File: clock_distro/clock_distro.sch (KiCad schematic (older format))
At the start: 37 parts, among them J1 SMA, J10 SMA, J2 SMA, J3 SMA, J4 SMA, J5 SMA, J6 SMA, J7 SMA, J8 SMA, J9 SMA, P1 CONN_01X02, U1 CDCLVC1108

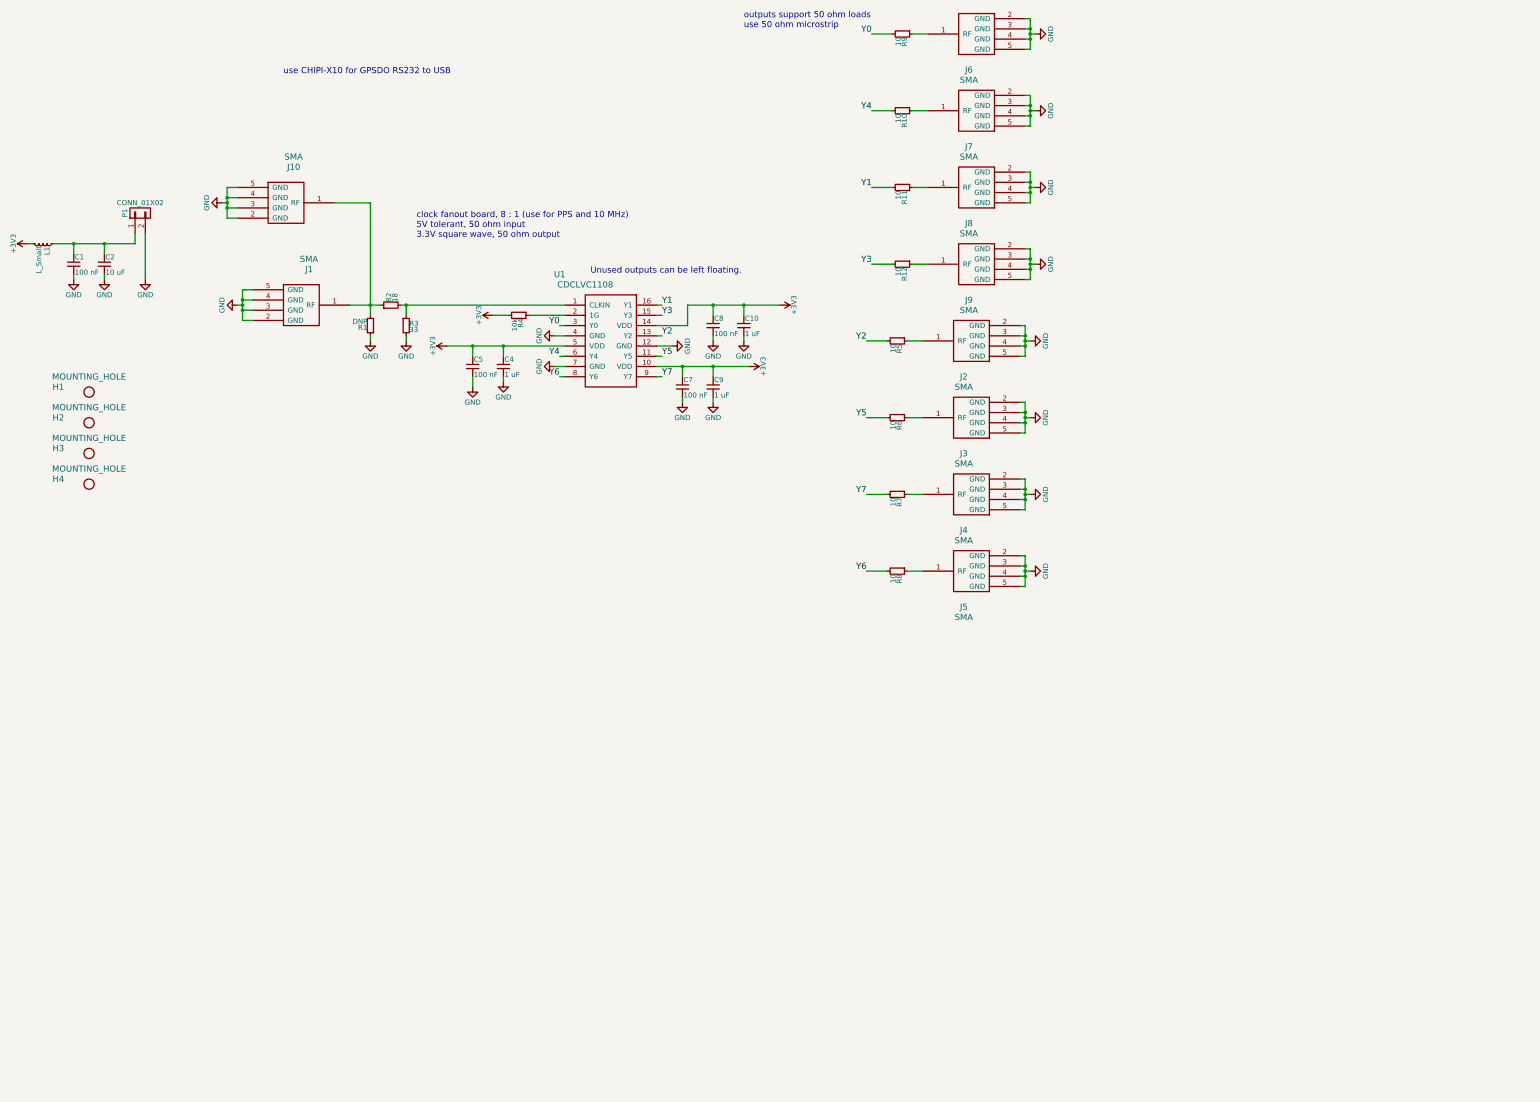
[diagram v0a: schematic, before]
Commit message: added bc637 pcie dsub15 clock/pps breakout
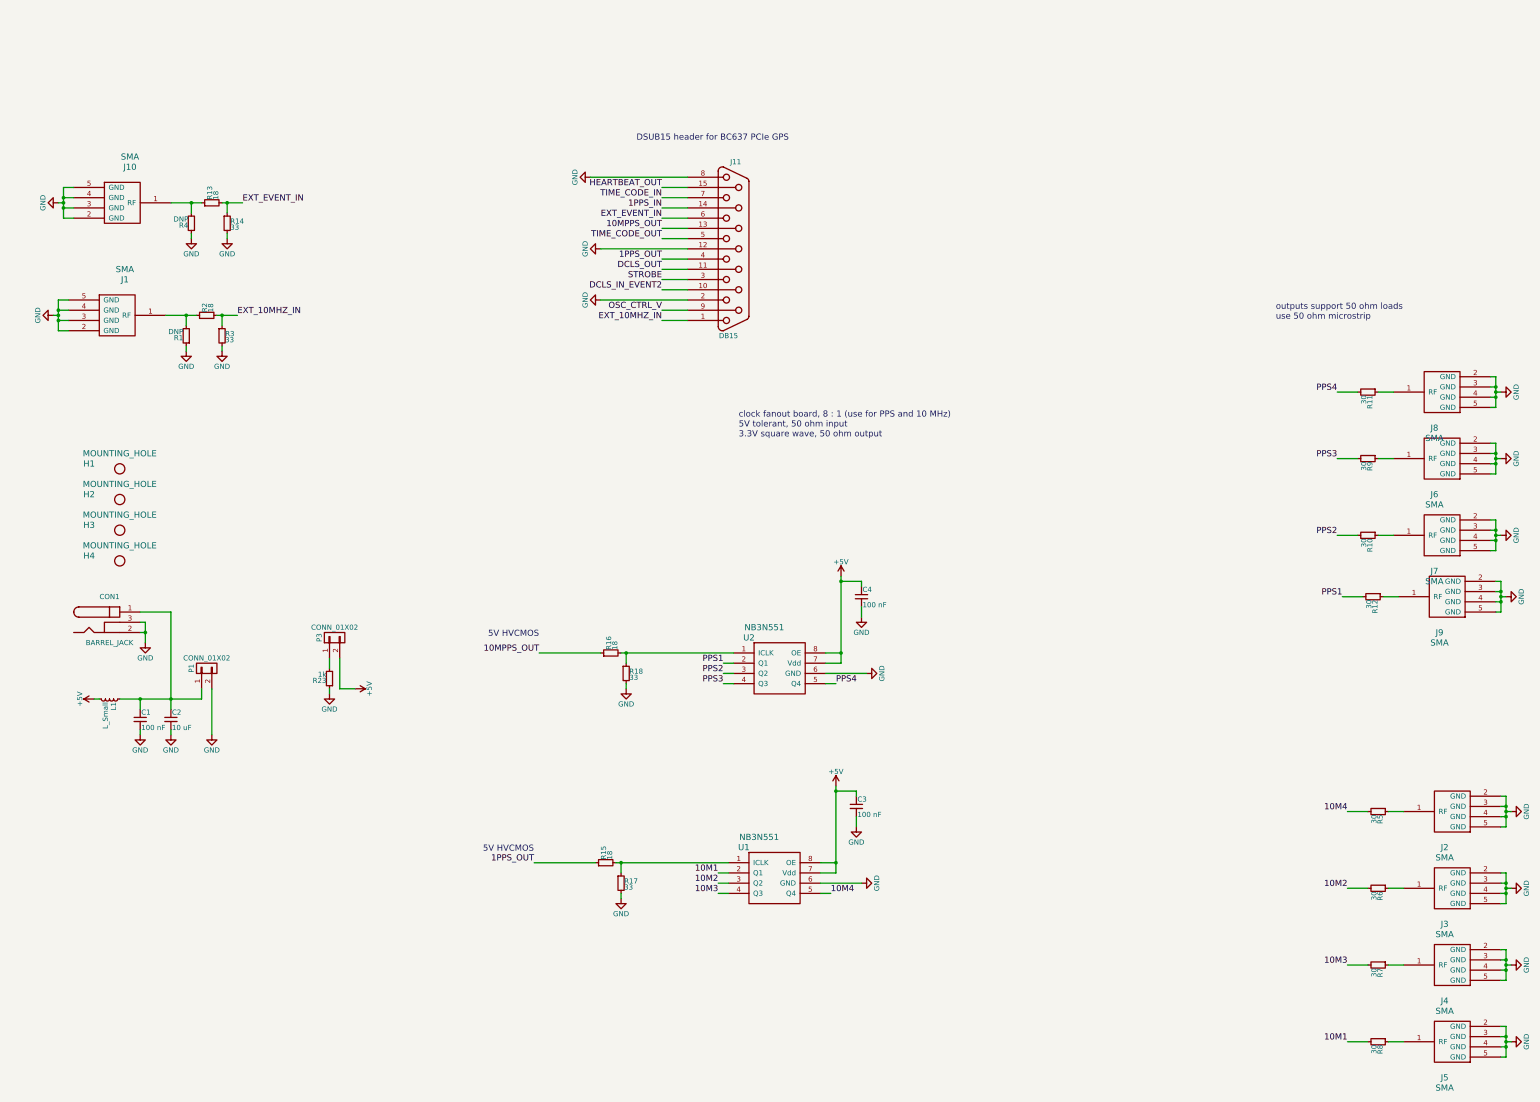
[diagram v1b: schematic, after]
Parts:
- removed C10, C9: 1 uF, Capacitors_SMD:C_0603, symbol C_Small
- removed C5, C7, C8: 100 nF, Capacitors_SMD:C_0603, symbol C_Small
- removed U1: CDCLVC1108, Housings_SSOP:TSSOP-16_4.4x5mm_Pitch0.65mm, symbol CDCLVC1108
- added C3: 100 nF, Capacitors_SMD:C_0603, symbol C_Small
- added CON1: BARREL_JACK, Connect:BARREL_JACK, symbol BARREL_JACK
- added J11: DB15, Connect:DB15FC, symbol DB15
- added P3: CONN_01X02, Connect:PINHEAD1-2, symbol CONN_01X02
- added R13, R15, R16: 18, Resistors_SMD:R_0603, symbol R_Small
- added R14, R17, R18: 33, Resistors_SMD:R_0603, symbol R_Small
- added R23: 1k, Resistors_SMD:R_0603, symbol R_Small
- added U1, U2: NB3N551, Housings_SOIC:SOIC-8_3.9x4.9mm_Pitch1.27mm, symbol NB3N551
- C4: value 1 uF -> 100 nF
- R10, R11, R12, R5, R6, R7, R8, R9: value 10 -> 30
- R4: value 10k -> DNP
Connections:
- net GND: now also R4.1, C3.2, CON1.2, CON1.3, J11.12 (P12), J11.2, J11.8, R14.2, R17.2, R18.2, R23.1, U1.6 (GND), U2.6 (GND)
- net EXT_10MHZ_IN: now reaches R2.2, R3.1
- net EXT_10MHZ_IN: now also J11.1
- net at C1.1, C2.1, L1.1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: now also CON1.1
- net at J1.1 (RF), R1.2, R2.1: no longer J10.1 (RF)
- net +3V3 renamed +5V
- net +5V: now also C3.1, P3.2 (P2), U1.7 (Vdd), U1.8 (OE), U2.7 (Vdd), U2.8 (OE); no longer R4.2
- net Y0 renamed PPS3
- net PPS3: now also U2.4 (Q3)
- net Y1 renamed PPS4
- net PPS4: now also U2.5 (Q4)
- net Y2 renamed 10M4
- net 10M4: now also U1.5 (Q4)
- net Y3 renamed PPS1
- net PPS1: now also U2.2 (Q1)
- net Y4 renamed PPS2
- net PPS2: now also U2.3 (Q2)
- net Y5 renamed 10M2
- net 10M2: now also U1.3 (Q2)
- net Y6 renamed 10M1
- net 10M1: now also U1.2 (Q1)
- net Y7 renamed 10M3
- net 10M3: now also U1.4 (Q3)
- new net: R16.2, R18.1, U2.1 (ICLK)
- new net: R15.2, R17.1, U1.1 (ICLK)
- new net: J10.1 (RF), R13.1, R4.2
- new net: P3.1 (P1), R23.2
- new net 10MPPS_OUT: J11.13 (P13), R16.1
- new net 1PPS_IN: J11.14 (P14)
- new net 1PPS_OUT: J11.4, R15.1
- new net DCLS_IN_EVENT2: J11.10 (P10)
- new net DCLS_OUT: J11.11 (P111)
- new net EXT_EVENT_IN: J11.6, R13.2, R14.1
- new net HEARTBEAT_OUT: J11.15 (P15)
- new net OSC_CTRL_V: J11.9 (P9)
- new net STROBE: J11.3
- new net TIME_CODE_IN: J11.7
- new net TIME_CODE_OUT: J11.5
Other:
- note added: "5V HVCMOS"
- note added: "DSUB15 header for BC637 PCIe GPS"
- note removed: "Unused outputs can be left floating."
- note removed: "use CHIPI-X10 for GPSDO RS232 to USB"
- moved on the sheet: C1, C2, H1, H2, H3, H4, J1, J2, J3, J4, J5, J6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

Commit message: length tuned clock/pps traces, switch dsub15 connector to male
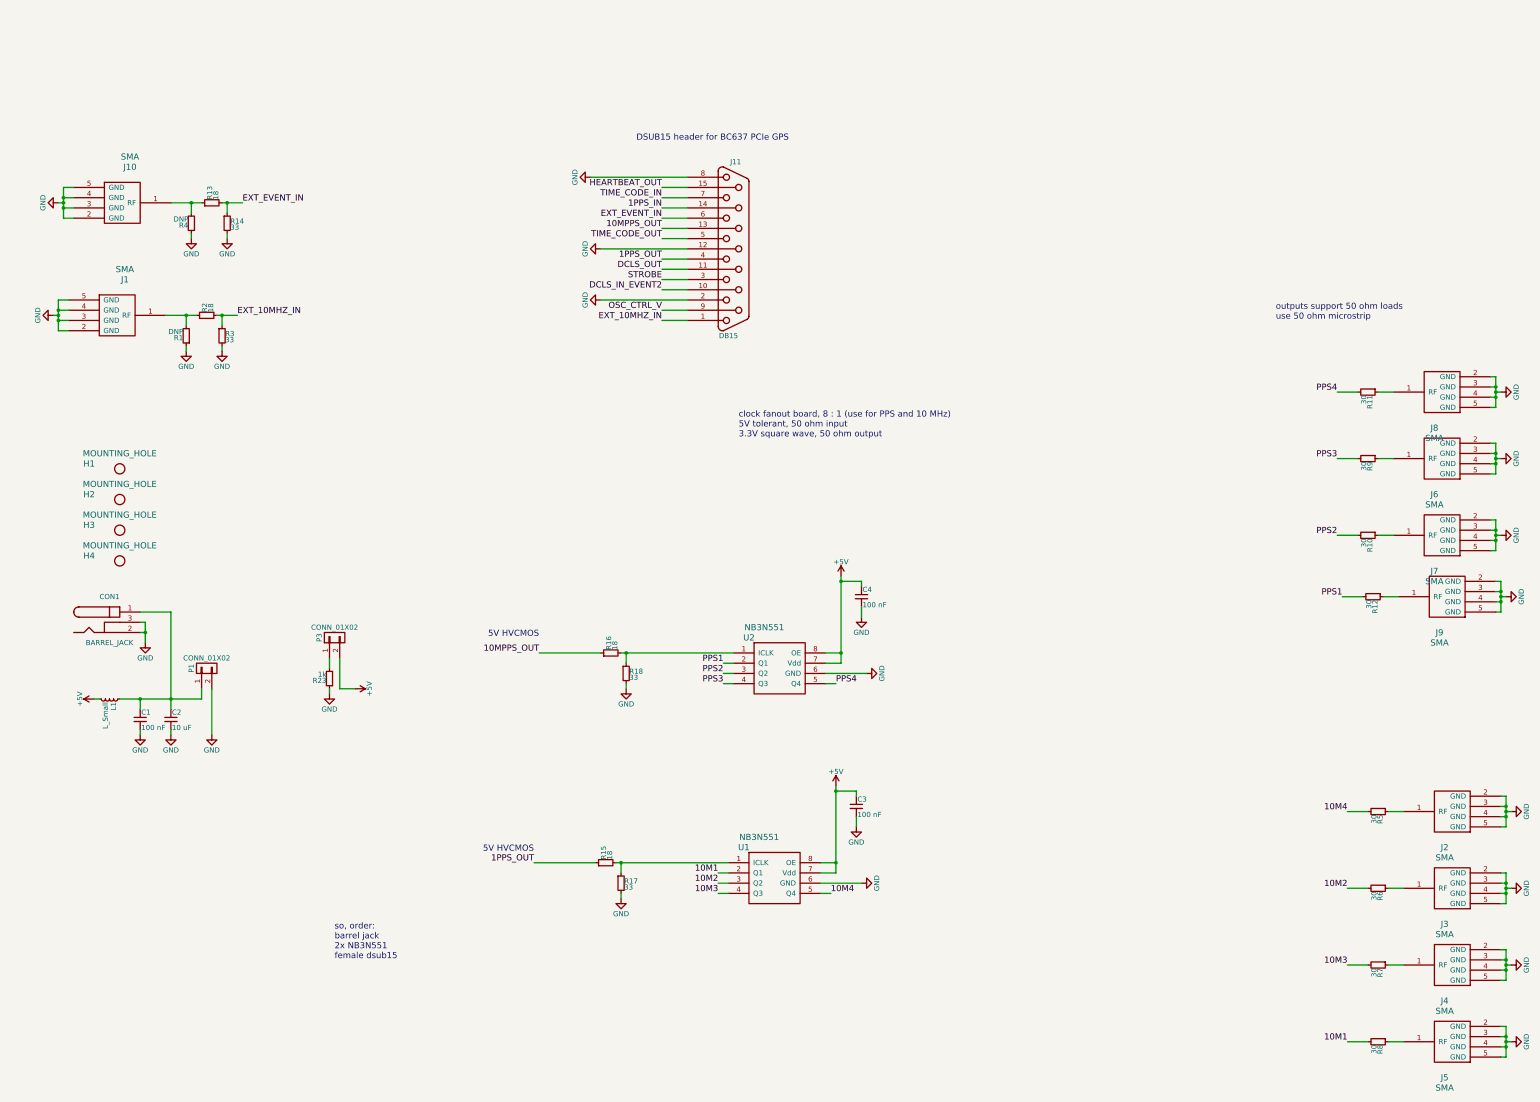
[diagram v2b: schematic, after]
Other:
- note added: "so, order:\nbarrel jack\n2x NB3N551\nfemale dsub15"
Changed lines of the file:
@@
 Connection ~ 2250 7250
 Wire Wire Line
-	2250 6400 2250 7250
-Wire Wire Line
-	2250 7250 2250 7350
+	2250 6400 2250 7350
 Wire Wire Line
 	2250 7600 2250 7550
@@
 	2550 7250 2550 7150
 Wire Wire Line
-	1750 7250 1950 7250
-Wire Wire Line
-	1950 7250 2250 7250
-Wire Wire Line
-	2250 7250 2550 7250
+	1750 7250 2550 7250
 Wire Wire Line
 	2650 7150 2650 7600
@@
 $EndComp
 Wire Wire Line
-	1100 3500 1150 3500
-Wire Wire Line
-	1150 3350 1150 3450
-Wire Wire Line
-	1150 3450 1150 3500
-Wire Wire Line
-	1150 3500 1150 3550
-Wire Wire Line
-	1150 3550 1150 3650
+	1150 3500 1100 3500
+Wire Wire Line
+	1150 3350 1150 3650
 Wire Wire Line
 	1150 3350 1250 3350
@@
 	2400 3800 2400 3850
 Wire Wire Line
-	2200 3500 2400 3500
-Wire Wire Line
-	2400 3500 2500 3500
+	2200 3500 2500 3500
 $Comp
 L GND #PWR06
@@
 	15150 4850 15200 4850
 Wire Wire Line
-	15200 4750 15200 4850
-Wire Wire Line
-	15200 4850 15200 4900
-Wire Wire Line
-	15200 4900 15200 4950
-Wire Wire Line
-	15200 4950 15200 5050
+	15200 4750 15200 5050
 Wire Wire Line
 	15200 4900 15250 4900
@@
 	15150 5600 15200 5600
 Wire Wire Line
-	15200 5500 15200 5600
-Wire Wire Line
-	15200 5600 15200 5650
-Wire Wire Line
-	15200 5650 15200 5700
-Wire Wire Line
-	15200 5700 15200 5800
+	15200 5500 15200 5800
 Wire Wire Line
 	15200 5650 15250 5650
@@
 	15150 4200 15200 4200
 Wire Wire Line
-	15200 4100 15200 4200
-Wire Wire Line
-	15200 4200 15200 4250
-Wire Wire Line
-	15200 4250 15200 4300
-Wire Wire Line
-	15200 4300 15200 4400
+	15200 4100 15200 4400
 Wire Wire Line
 	15200 4250 15250 4250
@@
 	15200 6200 15250 6200
 Wire Wire Line
-	15250 6100 15250 6200
-Wire Wire Line
-	15250 6200 15250 6250
-Wire Wire Line
-	15250 6250 15250 6300
-Wire Wire Line
-	15250 6300 15250 6400
+	15250 6100 15250 6400
 Wire Wire Line
 	15250 6250 15300 6250
@@
 	15250 8300 15300 8300
 Wire Wire Line
-	15300 8200 15300 8300
-Wire Wire Line
-	15300 8300 15300 8350
-Wire Wire Line
-	15300 8350 15300 8400
-Wire Wire Line
-	15300 8400 15300 8500
+	15300 8200 15300 8500
 Wire Wire Line
 	15300 8350 15350 8350
@@
 	15250 9050 15300 9050
 Wire Wire Line
-	15300 8950 15300 9050
-Wire Wire Line
-	15300 9050 15300 9100
-Wire Wire Line
-	15300 9100 15300 9150
-Wire Wire Line
-	15300 9150 15300 9250
+	15300 8950 15300 9250
 Wire Wire Line
 	15300 9100 15350 9100
@@
 	15250 9800 15300 9800
 Wire Wire Line
-	15300 9700 15300 9800
-Wire Wire Line
-	15300 9800 15300 9850
-Wire Wire Line
-	15300 9850 15300 9900
-Wire Wire Line
-	15300 9900 15300 10000
+	15300 9700 15300 10000
 Wire Wire Line
 	15300 9850 15350 9850
@@
 	15250 10550 15300 10550
 Wire Wire Line
-	15300 10450 15300 10550
-Wire Wire Line
-	15300 10550 15300 10600
-Wire Wire Line
-	15300 10600 15300 10650
-Wire Wire Line
-	15300 10650 15300 10750
+	15300 10450 15300 10750
 Wire Wire Line
 	15300 10600 15350 10600
@@
 EXT_10MHZ_IN
 Wire Wire Line
-	2700 3500 2750 3500
-Wire Wire Line
-	2750 3500 2900 3500
+	2700 3500 2900 3500
 Text Label 5850 6800 2    60   ~ 0
 10MPPS_OUT
@@
 Connection ~ 6700 6800
 Wire Wire Line
-	6650 6800 6700 6800
-Wire Wire Line
-	6700 6800 7750 6800
+	6650 6800 7750 6800
 Wire Wire Line
 	5850 6800 6450 6800
@@
 	9050 7000 8650 7000
 Wire Wire Line
-	8650 6900 8800 6900
-Wire Wire Line
-	8800 6900 8800 6800
-Wire Wire Line
-	8800 6800 8800 6100
-Wire Wire Line
-	8800 6100 8800 6050
+	8800 6900 8650 6900
+Wire Wire Line
+	8800 6050 8800 6900
 $Comp
 L C_Small C4
@@
 Connection ~ 6650 8850
 Wire Wire Line
-	6600 8850 6650 8850
-Wire Wire Line
-	6650 8850 7700 8850
+	6600 8850 7700 8850
 Wire Wire Line
 	5800 8850 6400 8850
@@
 	9000 9050 8600 9050
 Wire Wire Line
-	8600 8950 8750 8950
-Wire Wire Line
-	8750 8950 8750 8850
-Wire Wire Line
-	8750 8850 8750 8150
-Wire Wire Line
-	8750 8150 8750 8100
+	8750 8950 8600 8950
+Wire Wire Line
+	8750 8100 8750 8950
 $Comp
 L C_Small C3
@@
 $EndComp
 Wire Wire Line
-	1150 2400 1200 2400
-Wire Wire Line
-	1200 2250 1200 2350
-Wire Wire Line
-	1200 2350 1200 2400
-Wire Wire Line
-	1200 2400 1200 2450
-Wire Wire Line
-	1200 2450 1200 2550
+	1200 2400 1150 2400
+Wire Wire Line
+	1200 2250 1200 2550
 Wire Wire Line
 	1200 2250 1300 2250
@@
 	2450 2700 2450 2750
 Wire Wire Line
-	2250 2400 2450 2400
-Wire Wire Line
-	2450 2400 2550 2400
+	2250 2400 2550 2400
 $Comp
 L R_Small R13
@@
 	2450 2400 2450 2500
 Wire Wire Line
-	2750 2400 2800 2400
-Wire Wire Line
-	2800 2400 2950 2400
+	2750 2400 2950 2400
 $Comp
 L BARREL_JACK CON1
@@
 	1950 6600 2000 6600
 Wire Wire Line
-	2000 6500 2000 6600
-Wire Wire Line
-	2000 6600 2000 6700
+	2000 6500 2000 6700
 Wire Wire Line
 	1950 6500 2000 6500
@@
 Wire Wire Line
 	3900 7150 3900 6850
+Text Notes 3850 9800 0    60   ~ 0
+so, order:\nbarrel jack\n2x NB3N551\nfemale dsub15
 $EndSCHEMATC

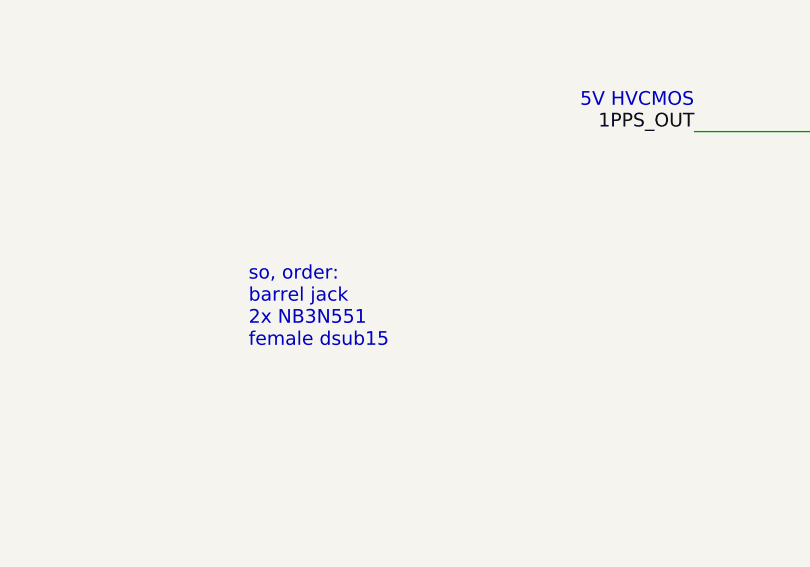
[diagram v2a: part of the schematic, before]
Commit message: fixed dsub 15 connector footprint - moved mounting holes
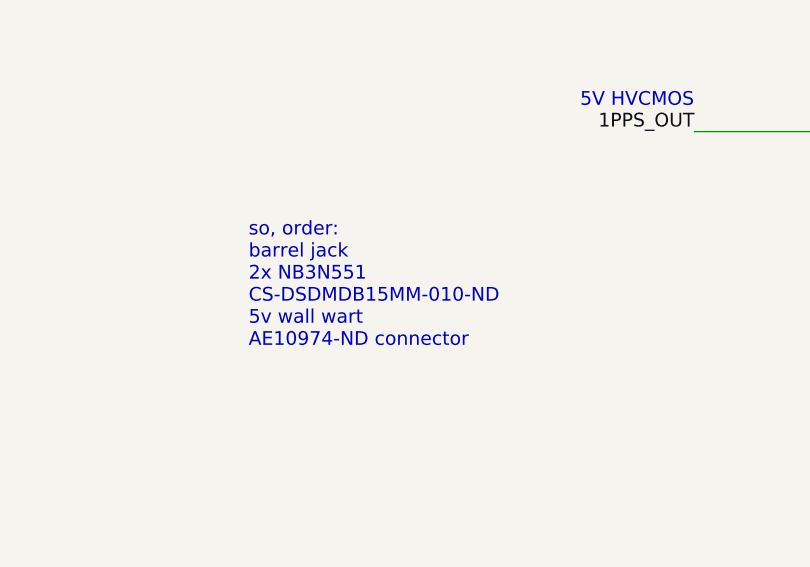
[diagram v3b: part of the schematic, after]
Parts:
- J11: footprint Connect:DB15FC -> Connect:DB15MC
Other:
- note added: "so, order:\nbarrel jack\n2x NB3N551\nCS-DSDMDB15MM-010-ND\n5v wall wart\nAE10974-ND connector"
- note removed: "so, order:\nbarrel jack\n2x NB3N551\nfemale dsub15"
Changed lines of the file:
@@
 F 0 "J11" H 7770 3700 50  0000 C CNN
 F 1 "DB15" H 7700 2000 50  0000 C CNN
-F 2 "Connect:DB15FC" H 7750 2850 50  0001 C CNN
+F 2 "Connect:DB15MC" H 7750 2850 50  0001 C CNN
 F 3 "" H 7750 2850 50  0000 C CNN
 	1    7750 2850
@@
 	3900 7150 3900 6850
 Text Notes 3850 9800 0    60   ~ 0
-so, order:\nbarrel jack\n2x NB3N551\nfemale dsub15
+so, order:\nbarrel jack\n2x NB3N551\nCS-DSDMDB15MM-010-ND\n5v wall wart\nAE10974-ND connector
 $EndSCHEMATC
